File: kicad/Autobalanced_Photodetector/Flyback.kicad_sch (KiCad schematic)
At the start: 0 parts

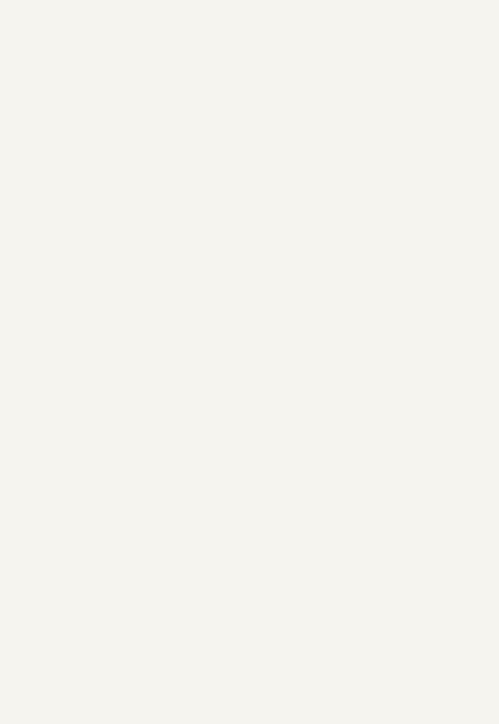
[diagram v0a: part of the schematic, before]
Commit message: feat(kicad): add HV regulators and reference control
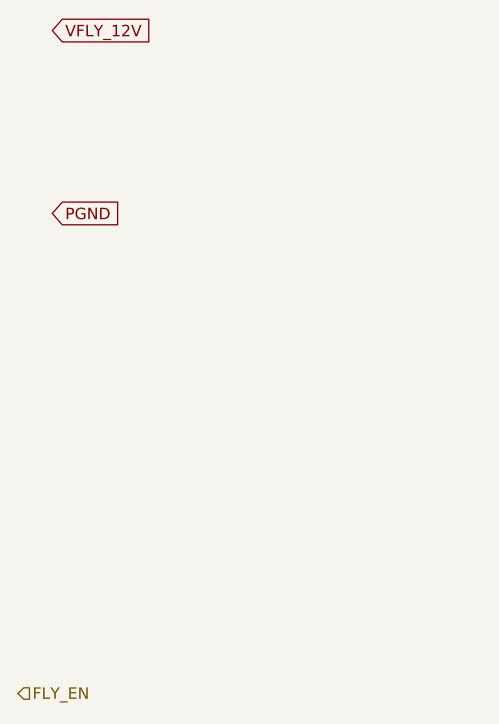
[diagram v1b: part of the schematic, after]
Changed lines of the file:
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@@
 (kicad_sch (version 20230121) (generator eeschema)
   (paper "A4")
+  (global_label "VFLY_12V" (shape input) (at 27.94 54.61 0) (fields_autoplaced)
+    (effects (font (size 1.27 1.27)) (justify left))
+    (property "Intersheetrefs" "${INTERSHEET_REFS}" (at 39.6943 54.61 0)
+      (effects (font (size 1.27 1.27)) (justify left) hide)
+    )
+  )
+  (global_label "PGND" (shape input) (at 27.94 74.93 0) (fields_autoplaced)
+    (effects (font (size 1.27 1.27)) (justify left))
+    (property "Intersheetrefs" "${INTERSHEET_REFS}" (at 36.0657 74.93 0)
+      (effects (font (size 1.27 1.27)) (justify left) hide)
+    )
+  )
+  (hierarchical_label "FLY_EN" (shape input) (at 24.13 128.27 0) (fields_autoplaced)
+    (effects (font (size 1.27 1.27)) (justify left))
+  )
   (hierarchical_label "HV_RAW_POS" (shape output) (at 267.97 55.88 0) (fields_autoplaced)
     (effects (font (size 1.27 1.27)) (justify left))
